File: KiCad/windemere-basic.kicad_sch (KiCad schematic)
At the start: 53 parts, among them J1 Barrel_Jack, SW1 Push_Button, SW2 SW_SPDT, U1 HD44780U, U2 WD65C02, U3 28C256, U4 62256, U5 WD65C22, U6 74HC00, U7 MM74C922, U8 L7805, X1 1MHz

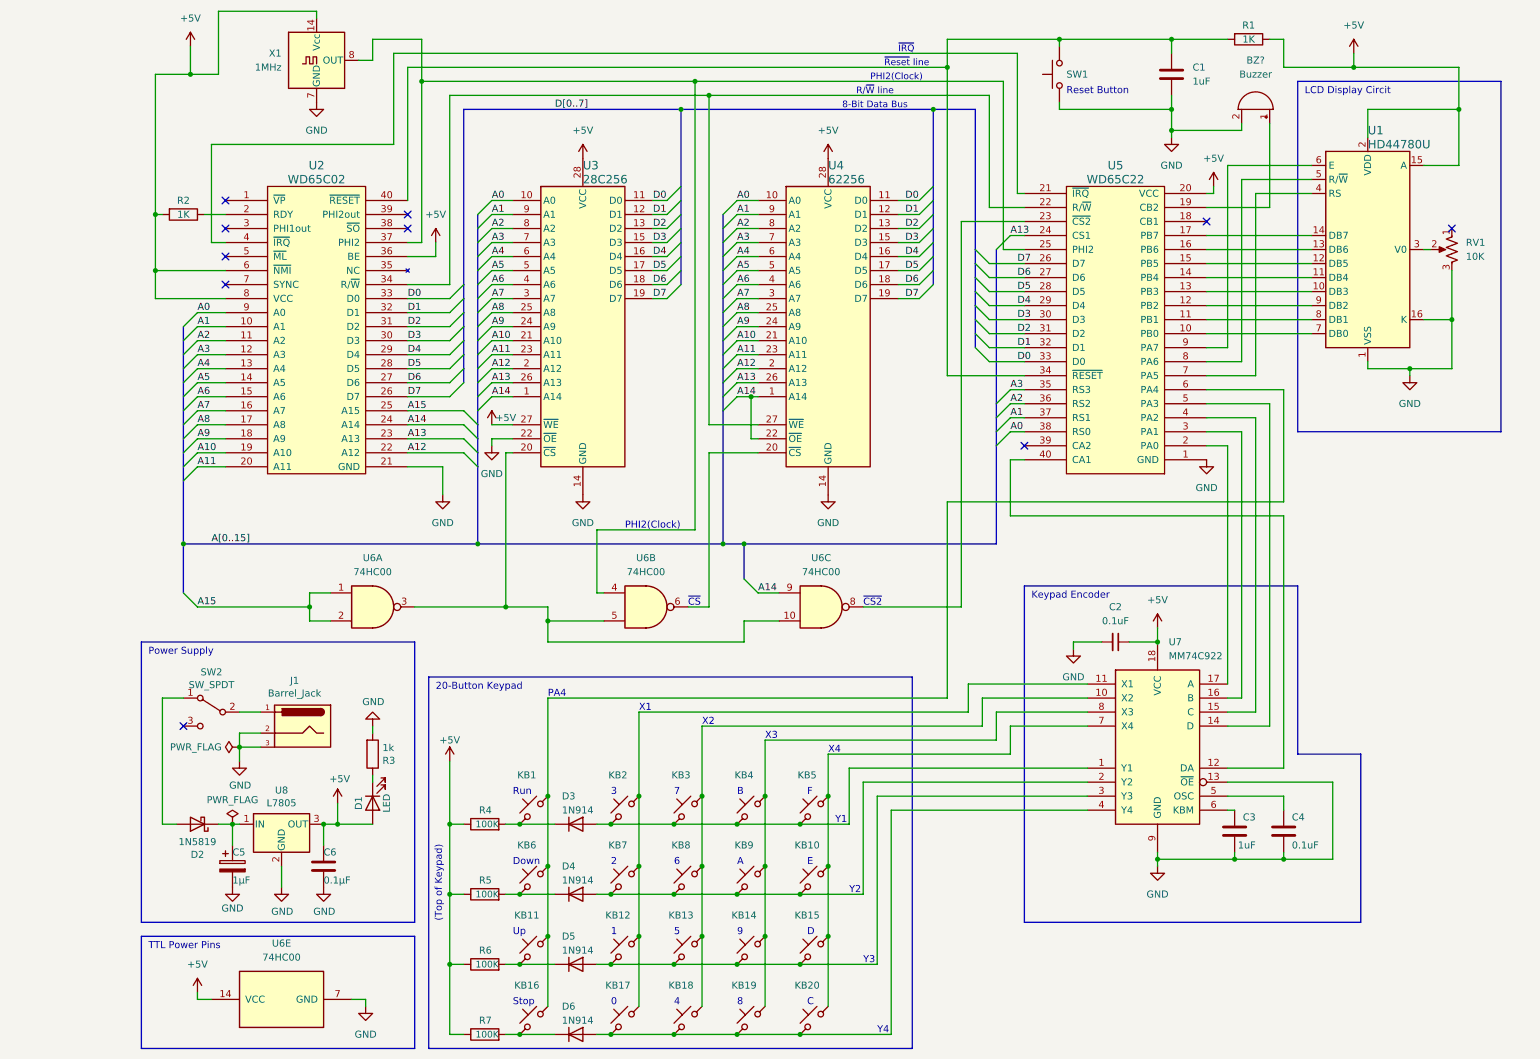
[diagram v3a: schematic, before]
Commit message: Add J1
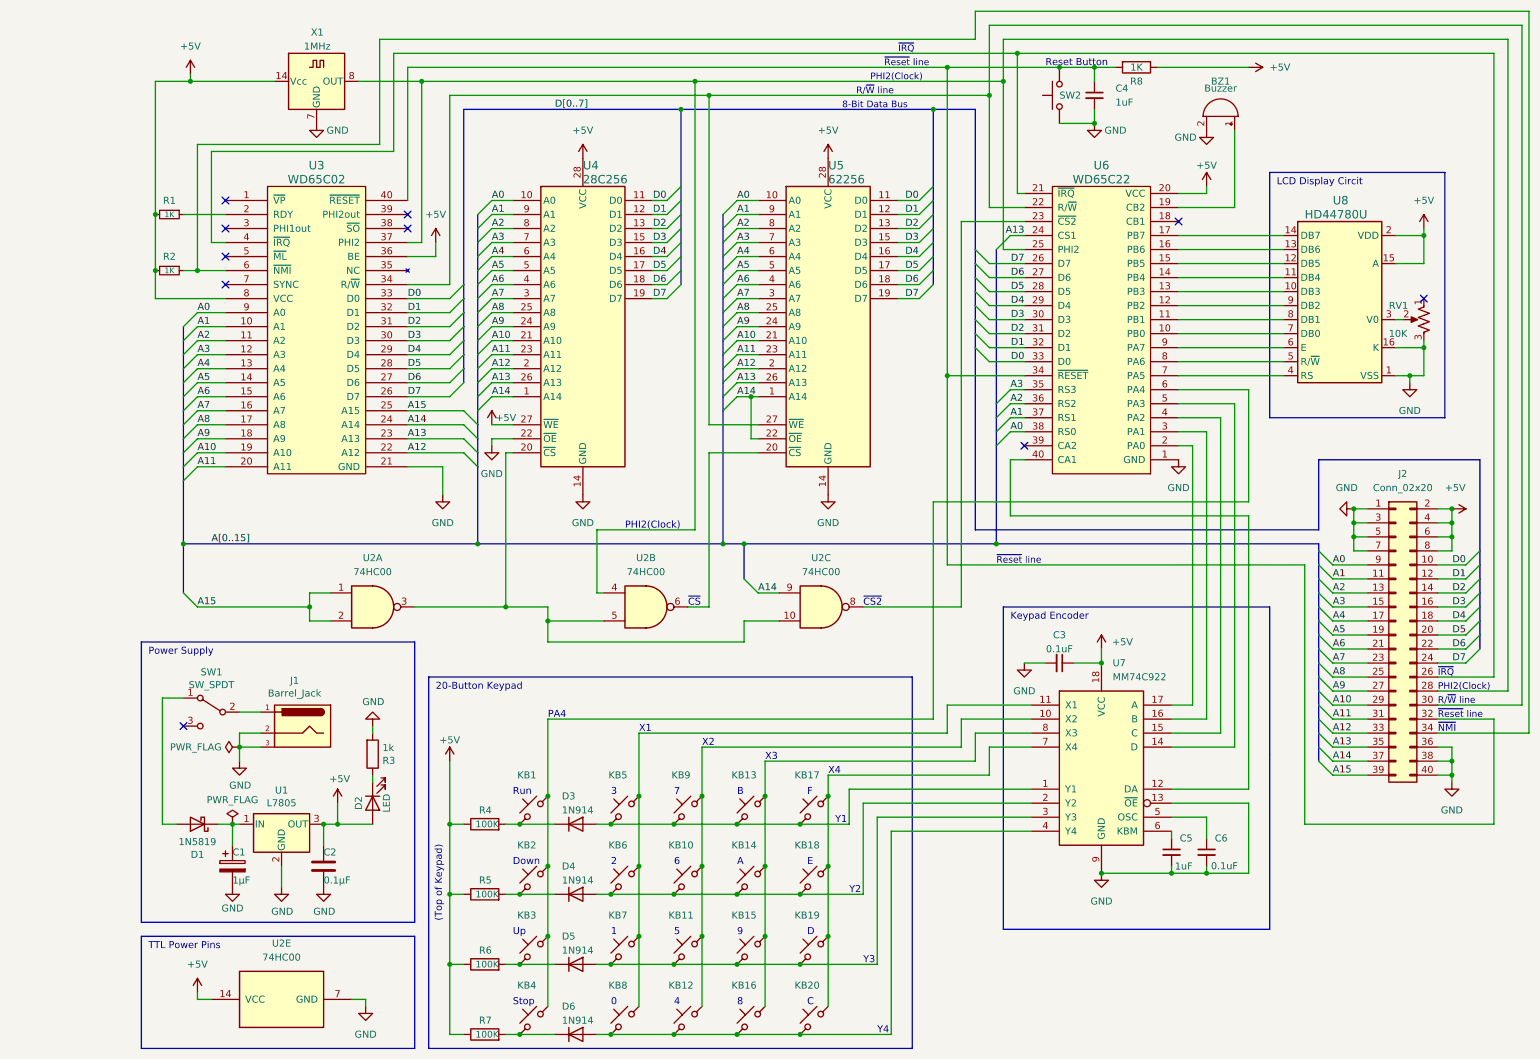
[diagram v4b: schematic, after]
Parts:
- removed U1: HD44780U, Display:WC1602A, symbol Display_Character:LCD-016N002L
- added J2: Conn_02x20, Connector_PinHeader_2.54mm:PinHeader_2x20_P2.54mm_Vertical, symbol Connector_Generic:Conn_02x20_Odd_Even
- added R2: 1K, Resistor_THT:R_Axial_DIN0207_L6.3mm_D2.5mm_P10.16mm_Horizontal, symbol Device:R_Small
- added U8: HD44780U, Display:WC1602A, symbol Display_Character:LCD-016N002L
- BZ1: renamed from BZ?; footprint (none) -> Buzzer_Beeper:Buzzer_12x9.5RM7.6
- C2: renamed from C6; footprint Capacitor_THT:C_Disc_D5.0mm_W2.5mm_P2.50mm -> Capacitor_THT:C_Disc_D7.0mm_W2.5mm_P5.00mm
- C4: renamed from C1; footprint Capacitor_THT:C_Disc_D5.0mm_W2.5mm_P2.50mm -> Capacitor_THT:C_Disc_D7.0mm_W2.5mm_P5.00mm; symbol Device:C -> Device:C_Small
- C5: renamed from C3; symbol Device:C -> Device:C_Small
- C6: renamed from C4; symbol Device:C -> Device:C_Small
- R1: renamed from R2; footprint Resistor_THT:R_Axial_DIN0204_L3.6mm_D1.6mm_P7.62mm_Horizontal -> Resistor_THT:R_Axial_DIN0207_L6.3mm_D2.5mm_P10.16mm_Horizontal; symbol Device:R -> Device:R_Small
- R3: footprint Resistor_THT:R_Axial_DIN0204_L3.6mm_D1.6mm_P7.62mm_Horizontal -> Resistor_THT:R_Axial_DIN0207_L6.3mm_D2.5mm_P10.16mm_Horizontal
- R8: renamed from R1; footprint Resistor_THT:R_Axial_DIN0204_L3.6mm_D1.6mm_P7.62mm_Horizontal -> Resistor_THT:R_Axial_DIN0207_L6.3mm_D2.5mm_P10.16mm_Horizontal
- SW2: renamed from SW1; value Push_Button -> Push_Button_small
- renumbered C5 to C1, C2 to C3, D2 to D1, D1 to D2, KB8 to KB10, KB13 to KB11, KB18 to KB12, KB4 to KB13, KB9 to KB14, KB14 to KB15, KB19 to KB16, KB5 to KB17, KB10 to KB18, KB15 to KB19, KB6 to KB2, KB11 to KB3, KB16 to KB4, KB2 to KB5, KB7 to KB6, KB12 to KB7, KB17 to KB8, KB3 to KB9, SW2 to SW1, U8 to U1, U6 to U2, U2 to U3, U3 to U4, U4 to U5, U5 to U6
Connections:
- net +5V: now also J2.2 (Pin_2), J2.4 (Pin_4), J2.6 (Pin_6), J2.8 (Pin_8), R2.2, U8.15 (A), U8.2 (VDD); no longer U3.6 (~{NMI})
- net A0: now also J2.9 (Pin_9)
- net A1: now also J2.11 (Pin_11)
- net A10: now also J2.29 (Pin_29)
- net A11: now also J2.31 (Pin_31)
- net A12: now also J2.33 (Pin_33)
- net A13: now also J2.35 (Pin_35)
- net A14: now also J2.37 (Pin_37)
- net A15: now also J2.39 (Pin_39)
- net A2: now also J2.13 (Pin_13)
- net A3: now also J2.15 (Pin_15)
- net A4: now also J2.17 (Pin_17)
- net A5: now also J2.19 (Pin_19)
- net A6: now also J2.21 (Pin_21)
- net A7: now also J2.23 (Pin_23)
- net A8: now also J2.25 (Pin_25)
- net A9: now also J2.27 (Pin_27)
- net D0: now also J2.10 (Pin_10)
- net D1: now also J2.12 (Pin_12)
- net D2: now also J2.14 (Pin_14)
- net D3: now also J2.16 (Pin_16)
- net D4: now also J2.18 (Pin_18)
- net D5: now also J2.20 (Pin_20)
- net D6: now also J2.22 (Pin_22)
- net D7: now also J2.24 (Pin_24)
- net GND: now also J2.1 (Pin_1), J2.3 (Pin_3), J2.36 (Pin_36), J2.38 (Pin_38), J2.40 (Pin_40), J2.5 (Pin_5), J2.7 (Pin_7), U8.1 (VSS), U8.16 (K)
- net at RV1.2: now also U8.3 (V0)
- net at U2.4, U3.37 (PHI2), U6.25 (PHI2)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: now also J2.28 (Pin_28)
- net at U3.34 (R/~{W}), U5.27 (~{WE}), U6.22 (R/~{W}): now also J2.30 (Pin_30)
- net at U3.4 (~{IRQ}), U6.21 (~{IRQ}): now also J2.26 (Pin_26)
- net at C4.1, R8.2, SW2.2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: now also J2.32 (Pin_32)
- net at U6.10 (PB0): now also U8.7 (DB0)
- net at U6.11 (PB1): now also U8.8 (DB1)
- net at U6.12 (PB2): now also U8.9 (DB2)
- net at U6.13 (PB3): now also U8.10 (DB3)
- net at U6.14 (PB4): now also U8.11 (DB4)
- net at U6.15 (PB5): now also U8.12 (DB5)
- net at U6.16 (PB6): now also U8.13 (DB6)
- net at U6.17 (PB7): now also U8.14 (DB7)
- net at U6.7 (PA5): now also U8.4 (RS)
- net at U6.8 (PA6): now also U8.5 (R/~{W})
- net at U6.9 (PA7): now also U8.6 (E)
- new net: J2.34 (Pin_34), R2.1, U3.6 (~{NMI})
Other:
- note added: "~{NMI}"
- moved on the sheet: BZ1, C3, C4, C5, C6, R1, R8, RV1, SW2, U6, U7, X1

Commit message: Added MCP102-475 to reset line
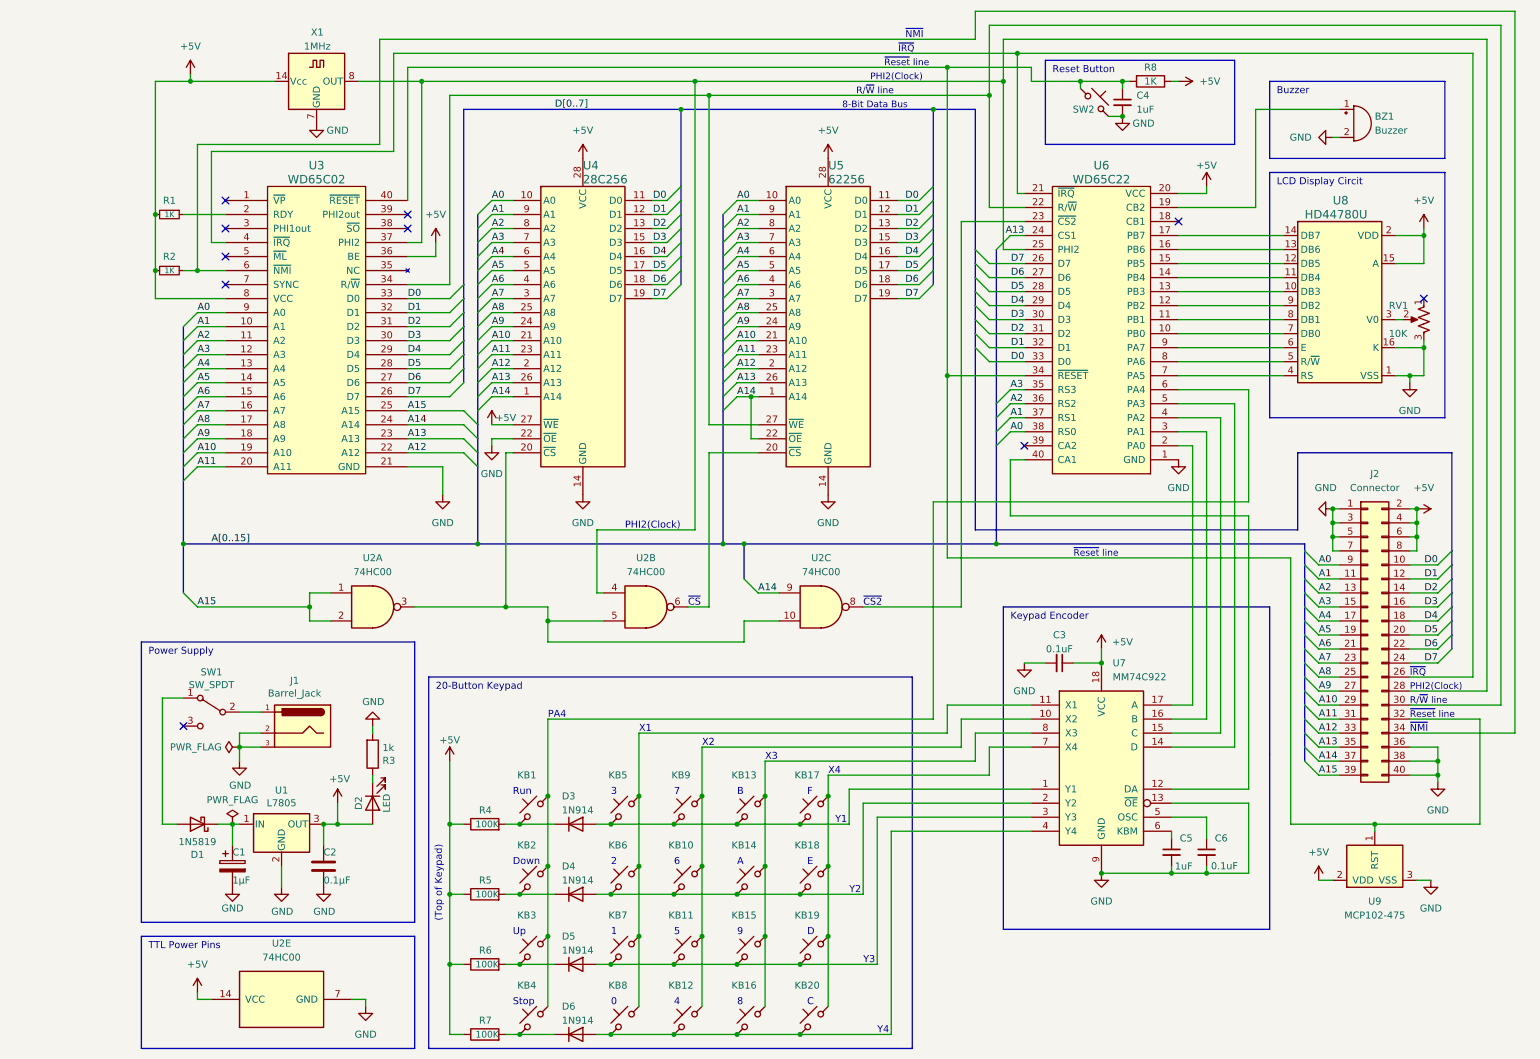
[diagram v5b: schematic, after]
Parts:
- added U9: MCP102-475, Package_TO_SOT_THT:TO-92, symbol Power_Supervisor:MCP101-475D
- J2: value Conn_02x20 -> Connector
- SW2: symbol Switch:SW_Push -> Switch:SW_Push_45deg
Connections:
- net +5V: now also U9.2 (VDD)
- net GND: now also U9.3 (VSS)
- net at C4.1, J2.32 (Pin_32), R8.2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: now also U9.1 (RST)
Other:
- note added: "Buzzer"
- moved on the sheet: BZ1, C4, J2, R8, SW2

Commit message: Add Digikey Part Numbers
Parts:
- BZ1: Digikey Part (none) -> 102-1156-ND
- C2: value 0.1µF -> 0.1uF; Digikey Part (none) -> 399-9877-1-ND
- C3, C6: footprint Capacitor_THT:C_Disc_D5.0mm_W2.5mm_P2.50mm -> Capacitor_THT:C_Disc_D7.0mm_W2.5mm_P5.00mm; Digikey Part (none) -> 399-9877-1-ND
- C4: Digikey Part (none) -> 399-13743-1-ND
- C5: footprint Capacitor_THT:C_Disc_D5.0mm_W2.5mm_P2.50mm -> Capacitor_THT:C_Disc_D7.0mm_W2.5mm_P5.00mm; Digikey Part (none) -> 399-13743-1-ND
- D1: Digikey Part (none) -> 1N5819GOS-ND
- R1, R2, R8: Digikey Part (none) -> CF14JT1K00CT-ND
- R3: value 1k -> 1K; Digikey Part (none) -> CF14JT1K00CT-ND
- R4, R5, R6, R7: Digikey Part (none) -> CF14JT100KCT-ND
- U1: Digikey Part (none) -> 497-1443-5-ND
- U2: Digikey Part (none) -> 2156-CD74HC00E-HC-ND
- U4: Digikey Part (none) -> AT28C256-15PU-ND
- U5: Digikey Part (none) -> 1450-1033-ND
- U7: Digikey Part (none) -> MM74C922N-ND
- U8: Digikey Part (none) -> 2470-ACM1602KC-NLW-BBW-R-ND
- U9: Digikey Part (none) -> MCP102-475E/TO-ND
- X1: Digikey Part (none) -> X937-ND

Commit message: Update windemere-basic.kicad_sch
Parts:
- C1: Digikey Part (none) -> 493-11321-3-ND
- D2: value LED -> LED_Red; Digikey Part (none) -> 160-1087-ND
- D3, D4, D5, D6: Digikey Part (none) -> 1N914FS-ND
- J1: Digikey Part (none) -> CP-018H-ND
- J2: Digikey Part (none) -> 732-5310-ND
- KB1, KB10, KB11, KB12, KB13, KB14, KB15, KB16, KB17, KB18, KB19, KB2, KB20, KB3, KB4, KB5, KB6, KB7, KB8, KB9: Digikey Part (none) -> CH162-ND
- RV1: Digikey Part (none) -> 490-2875-ND
- SW2: value Push_Button_small -> Push_Button; footprint Button_Switch_THT:SW_PUSH_6mm -> footprints:D6R90F1LFS; Digikey Part (none) -> 401-1978-ND

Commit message: Update windemere-basic.kicad_sch
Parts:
- U1: Mouser Part (none) -> 511-L7805CV
- U2: Mouser Part (none) -> 595-CD74HC00E
- U3: Mouser Part (none) -> 955-W65C02S6TPG-14
- U4: Mouser Part (none) -> 556-AT28C25615PU
- U5: Mouser Part (none) -> 913-AS6C62256-55PCN
- U6: Mouser Part (none) -> 955-W65C22S6TPG-14
- U9: Mouser Part (none) -> 579-MCP102-475E/TO
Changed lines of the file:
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@@
+      (effects (font (size 1.27 1.27)) hide)
+    )
+    (property "Mouser Part" "579-MCP102-475E/TO" (id 5) (at 238.76 168.91 0)
       (effects (font (size 1.27 1.27)) hide)
     )
@@
       (effects (font (size 1.27 1.27)) hide)
     )
+    (property "Mouser Part" "595-CD74HC00E" (id 5) (at 106.68 121.92 0)
+      (effects (font (size 1.27 1.27)) hide)
+    )
     (pin "4")
     (pin "5")
@@
     )
     (property "Digikey Part" "1450-1033-ND" (id 4) (at 139.7 71.12 0)
+      (effects (font (size 1.27 1.27)) hide)
+    )
+    (property "Mouser Part" "913-AS6C62256-55PCN" (id 5) (at 139.7 71.12 0)
       (effects (font (size 1.27 1.27)) hide)
     )
@@
       (effects (font (size 1.27 1.27)) hide)
     )
+    (property "Mouser Part" "595-CD74HC00E" (id 5) (at 40.64 193.04 0)
+      (effects (font (size 1.27 1.27)) hide)
+    )
     (pin "14")
     (pin "7")
@@
       (effects (font (size 1.524 1.524)) hide)
     )
-    (property "Datasheet" "" (id 3) (at 34.29 66.04 0)
+    (property "Datasheet" "https://www.mouser.com/datasheet/2/436/w65c02s-2572.pdf" (id 3) (at 34.29 66.04 0)
       (effects (font (size 1.524 1.524)))
     )
     (property "Digikey Part" "~" (id 4) (at 46.99 71.12 0)
+      (effects (font (size 1.27 1.27)) hide)
+    )
+    (property "Mouser Part" "955-W65C02S6TPG-14" (id 5) (at 46.99 71.12 0)
       (effects (font (size 1.27 1.27)) hide)
     )
@@
       (effects (font (size 1.27 1.27)) hide)
     )
+    (property "Mouser Part" "595-CD74HC00E" (id 5) (at 138.43 121.92 0)
+      (effects (font (size 1.27 1.27)) hide)
+    )
     (pin "10")
     (pin "8")
@@
       (effects (font (size 1.524 1.524)) hide)
     )
-    (property "Datasheet" "" (id 3) (at 179.07 67.31 0)
+    (property "Datasheet" "https://www.mouser.com/datasheet/2/436/w65c22-1197.pdf" (id 3) (at 179.07 67.31 0)
       (effects (font (size 1.524 1.524)))
     )
     (property "Digikey Part" "~" (id 4) (at 189.23 72.39 0)
+      (effects (font (size 1.27 1.27)) hide)
+    )
+    (property "Mouser Part" "955-W65C22S6TPG-14" (id 5) (at 189.23 72.39 0)
       (effects (font (size 1.27 1.27)) hide)
     )
@@
       (effects (font (size 1.27 1.27)) hide)
     )
+    (property "Mouser Part" "595-CD74HC00E" (id 5) (at 57.15 121.92 0)
+      (effects (font (size 1.27 1.27)) hide)
+    )
     (pin "1")
     (pin "2")
@@
       (effects (font (size 1.27 1.27)) hide)
     )
+    (property "Mouser Part" "511-L7805CV" (id 5) (at 40.64 161.29 0)
+      (effects (font (size 1.27 1.27)) hide)
+    )
     (pin "1")
     (pin "2")
@@
       (effects (font (size 1.27 1.27)) hide)
     )
+    (property "Mouser Part" "556-AT28C25615PU" (id 5) (at 95.25 71.12 0)
+      (effects (font (size 1.27 1.27)) hide)
+    )
